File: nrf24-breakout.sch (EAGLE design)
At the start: 4 parts, among them U1 NRF24

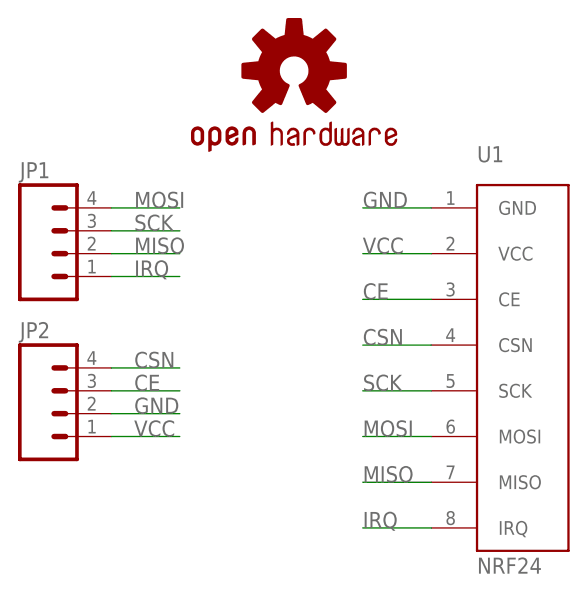
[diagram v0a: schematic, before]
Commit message: small aesthetic changes
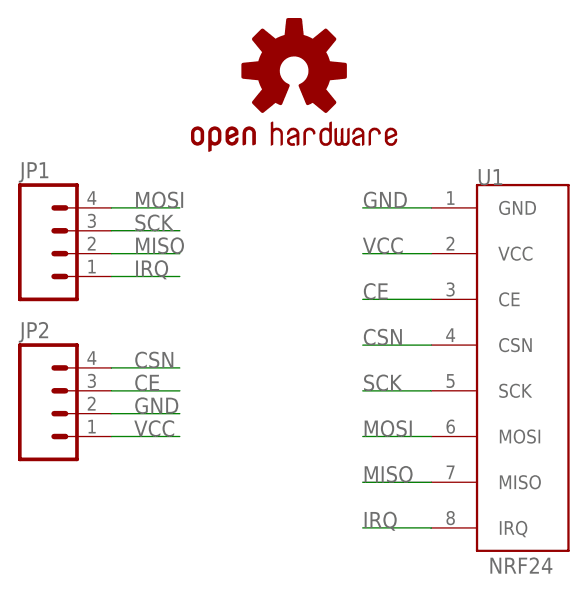
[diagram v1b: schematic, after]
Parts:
- JP1, JP2: PN (none) -> M20-9990446
- U1: PN (none) -> M20-7830446
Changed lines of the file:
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@@
 <grid distance="0.1" unitdist="inch" unit="inch" style="lines" multiple="1" display="no" altdistance="0.01" altunitdist="inch" altunit="inch"/>
 <layers>
-<layer number="1" name="Top" color="4" fill="1" visible="yes" active="no"/>
-<layer number="16" name="Bottom" color="1" fill="1" visible="yes" active="no"/>
-<layer number="17" name="Pads" color="2" fill="1" visible="yes" active="no"/>
-<layer number="18" name="Vias" color="2" fill="1" visible="yes" active="no"/>
-<layer number="19" name="Unrouted" color="6" fill="1" visible="yes" active="no"/>
-<layer number="20" name="Dimension" color="15" fill="1" visible="yes" active="no"/>
-<layer number="21" name="tPlace" color="7" fill="1" visible="yes" active="no"/>
-<layer number="22" name="bPlace" color="7" fill="1" visible="yes" active="no"/>
-<layer number="23" name="tOrigins" color="15" fill="1" visible="yes" active="no"/>
-<layer number="24" name="bOrigins" color="15" fill="1" visible="yes" active="no"/>
-<layer number="25" name="tNames" color="7" fill="1" visible="yes" active="no"/>
-<layer number="26" name="bNames" color="7" fill="1" visible="yes" active="no"/>
-<layer number="27" name="tValues" color="7" fill="1" visible="yes" active="no"/>
-<layer number="28" name="bValues" color="7" fill="1" visible="yes" active="no"/>
+<layer number="1" name="Top" color="4" fill="1" visible="no" active="no"/>
+<layer number="16" name="Bottom" color="1" fill="1" visible="no" active="no"/>
+<layer number="17" name="Pads" color="2" fill="1" visible="no" active="no"/>
+<layer number="18" name="Vias" color="2" fill="1" visible="no" active="no"/>
+<layer number="19" name="Unrouted" color="6" fill="1" visible="no" active="no"/>
+<layer number="20" name="Dimension" color="15" fill="1" visible="no" active="no"/>
+<layer number="21" name="tPlace" color="7" fill="1" visible="no" active="no"/>
+<layer number="22" name="bPlace" color="7" fill="1" visible="no" active="no"/>
+<layer number="23" name="tOrigins" color="15" fill="1" visible="no" active="no"/>
+<layer number="24" name="bOrigins" color="15" fill="1" visible="no" active="no"/>
+<layer number="25" name="tNames" color="7" fill="1" visible="no" active="no"/>
+<layer number="26" name="bNames" color="7" fill="1" visible="no" active="no"/>
+<layer number="27" name="tValues" color="7" fill="1" visible="no" active="no"/>
+<layer number="28" name="bValues" color="7" fill="1" visible="no" active="no"/>
 <layer number="29" name="tStop" color="7" fill="3" visible="no" active="no"/>
 <layer number="30" name="bStop" color="7" fill="6" visible="no" active="no"/>
@@
 <layer number="35" name="tGlue" color="7" fill="4" visible="no" active="no"/>
 <layer number="36" name="bGlue" color="7" fill="5" visible="no" active="no"/>
-<layer number="37" name="tTest" color="7" fill="1" visible="yes" active="no"/>
-<layer number="38" name="bTest" color="7" fill="1" visible="yes" active="no"/>
+<layer number="37" name="tTest" color="7" fill="1" visible="no" active="no"/>
+<layer number="38" name="bTest" color="7" fill="1" visible="no" active="no"/>
 <layer number="39" name="tKeepout" color="4" fill="11" visible="no" active="no"/>
 <layer number="40" name="bKeepout" color="1" fill="11" visible="no" active="no"/>
@@
 <layer number="44" name="Drills" color="7" fill="1" visible="no" active="no"/>
 <layer number="45" name="Holes" color="7" fill="1" visible="no" active="no"/>
-<layer number="46" name="Milling" color="3" fill="1" visible="yes" active="no"/>
-<layer number="47" name="Measures" color="7" fill="1" visible="yes" active="no"/>
-<layer number="48" name="Document" color="7" fill="1" visible="yes" active="no"/>
-<layer number="49" name="Reference" color="7" fill="1" visible="yes" active="no"/>
-<layer number="50" name="dxf" color="7" fill="1" visible="yes" active="no"/>
-<layer number="51" name="tDocu" color="7" fill="1" visible="yes" active="no"/>
-<layer number="52" name="bDocu" color="7" fill="1" visible="yes" active="no"/>
-<layer number="53" name="tGND_GNDA" color="7" fill="9" visible="yes" active="no"/>
-<layer number="54" name="bGND_GNDA" color="1" fill="9" visible="yes" active="no"/>
-<layer number="56" name="wert" color="7" fill="1" visible="yes" active="no"/>
-<layer number="57" name="tCAD" color="7" fill="1" visible="yes" active="no"/>
-<layer number="59" name="tCarbon" color="7" fill="1" visible="yes" active="no"/>
-<layer number="60" name="bCarbon" color="7" fill="1" visible="yes" active="no"/>
+<layer number="46" name="Milling" color="3" fill="1" visible="no" active="no"/>
+<layer number="47" name="Measures" color="7" fill="1" visible="no" active="no"/>
+<layer number="48" name="Document" color="7" fill="1" visible="no" active="no"/>
+<layer number="49" name="Reference" color="7" fill="1" visible="no" active="no"/>
+<layer number="50" name="dxf" color="7" fill="1" visible="no" active="no"/>
+<layer number="51" name="tDocu" color="7" fill="1" visible="no" active="no"/>
+<layer number="52" name="bDocu" color="7" fill="1" visible="no" active="no"/>
+<layer number="53" name="tGND_GNDA" color="7" fill="9" visible="no" active="no"/>
+<layer number="54" name="bGND_GNDA" color="1" fill="9" visible="no" active="no"/>
+<layer number="56" name="wert" color="7" fill="1" visible="no" active="no"/>
+<layer number="57" name="tCAD" color="7" fill="1" visible="no" active="no"/>
+<layer number="59" name="tCarbon" color="7" fill="1" visible="no" active="no"/>
+<layer number="60" name="bCarbon" color="7" fill="1" visible="no" active="no"/>
 <layer number="90" name="Modules" color="5" fill="1" visible="yes" active="yes"/>
 <layer number="91" name="Nets" color="2" fill="1" visible="yes" active="yes"/>
@@
 </classes>
 <parts>
-<part name="U1" library="nrf24" deviceset="NRF24" device=""/>
-<part name="JP1" library="SparkFun-Connectors" deviceset="M04" device="NO_SILK_ALL_ROUND"/>
-<part name="JP2" library="SparkFun-Connectors" deviceset="M04" device="NO_SILK_ALL_ROUND"/>
+<part name="U1" library="nrf24" deviceset="NRF24" device="">
+<attribute name="PN" value="M20-7830446"/>
+</part>
+<part name="JP1" library="SparkFun-Connectors" deviceset="M04" device="NO_SILK_ALL_ROUND">
+<attribute name="PN" value="M20-9990446"/>
+</part>
+<part name="JP2" library="SparkFun-Connectors" deviceset="M04" device="NO_SILK_ALL_ROUND">
+<attribute name="PN" value="M20-9990446"/>
+</part>
 <part name="LOGO1" library="SparkFun-Aesthetics" deviceset="OSHW-LOGO" device="S" value="OSHW-LOGOS"/>
 </parts>
@@
 </plain>
 <instances>
-<instance part="U1" gate="G$1" x="73.66" y="30.48"/>
-<instance part="JP1" gate="G$1" x="22.86" y="43.18"/>
-<instance part="JP2" gate="G$1" x="22.86" y="25.4"/>
+<instance part="U1" gate="G$1" x="73.66" y="30.48">
+<attribute name="PN" x="73.66" y="30.48" size="1.778" layer="96" display="off"/>
+</instance>
+<instance part="JP1" gate="G$1" x="22.86" y="43.18">
+<attribute name="PN" x="22.86" y="43.18" size="1.778" layer="96" display="off"/>
+</instance>
+<instance part="JP2" gate="G$1" x="22.86" y="25.4">
+<attribute name="PN" x="22.86" y="25.4" size="1.778" layer="96" display="off"/>
+</instance>
 <instance part="LOGO1" gate="G$1" x="48.26" y="63.5"/>
 </instances>
